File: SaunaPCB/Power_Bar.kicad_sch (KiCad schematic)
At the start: 54 parts, among them J201 KL3RM7.62, J202 KL3RM7.62, J203 KL3RM7.62, J204 KL2RM5.08, J205 KL3RM7.62, J206 KL3RM7.62, K201 Relais_SPDT_CO, K202 Relais_SPDT_CO, K203 Relais_SPDT_CO, K204 Relais_SPDT_CO, K205 Relais_SPDT_CO, K206 Relais_SPDT_CO, K207 Relais_SPDT_CO, U201 LHE05-20B24, U202 4N25, U203 4N25, U204 4N25, U302 LM2576T-5

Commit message: some step files added
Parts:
- renumbered C201 to C301, C202 to C302, C203 to C303, C204 to C304, C205 to C305, D201 to D301, D202 to D302, D301 to D303, D203 to D304, D204 to D305, D205 to D306, D206 to D307, D207 to D308, F201 to F301, H201 to H301, H202 to H302, H203 to H303, H204 to H304, H205 to H305, J201 to J301, J202 to J302, J203 to J303, J204 to J304, J205 to J305, J206 to J306, K201 to K301, K202 to K302, K203 to K303, K204 to K304, K205 to K305, K206 to K306, K207 to K307, L201 to L301, L202 to L302, L203 to L303, L203 to L304, R201 to R301, R202 to R302, R203 to R303, R204 to R304, R205 to R305, R206 to R306, R207 to R307, R208 to R308, R209 to R309, R210 to R310, R211 to R311, R212 to R312, R213 to R313, U201 to U301, U202 to U303, U203 to U304, U204 to U305
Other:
- moved on the sheet: D301, K301, K303, K305

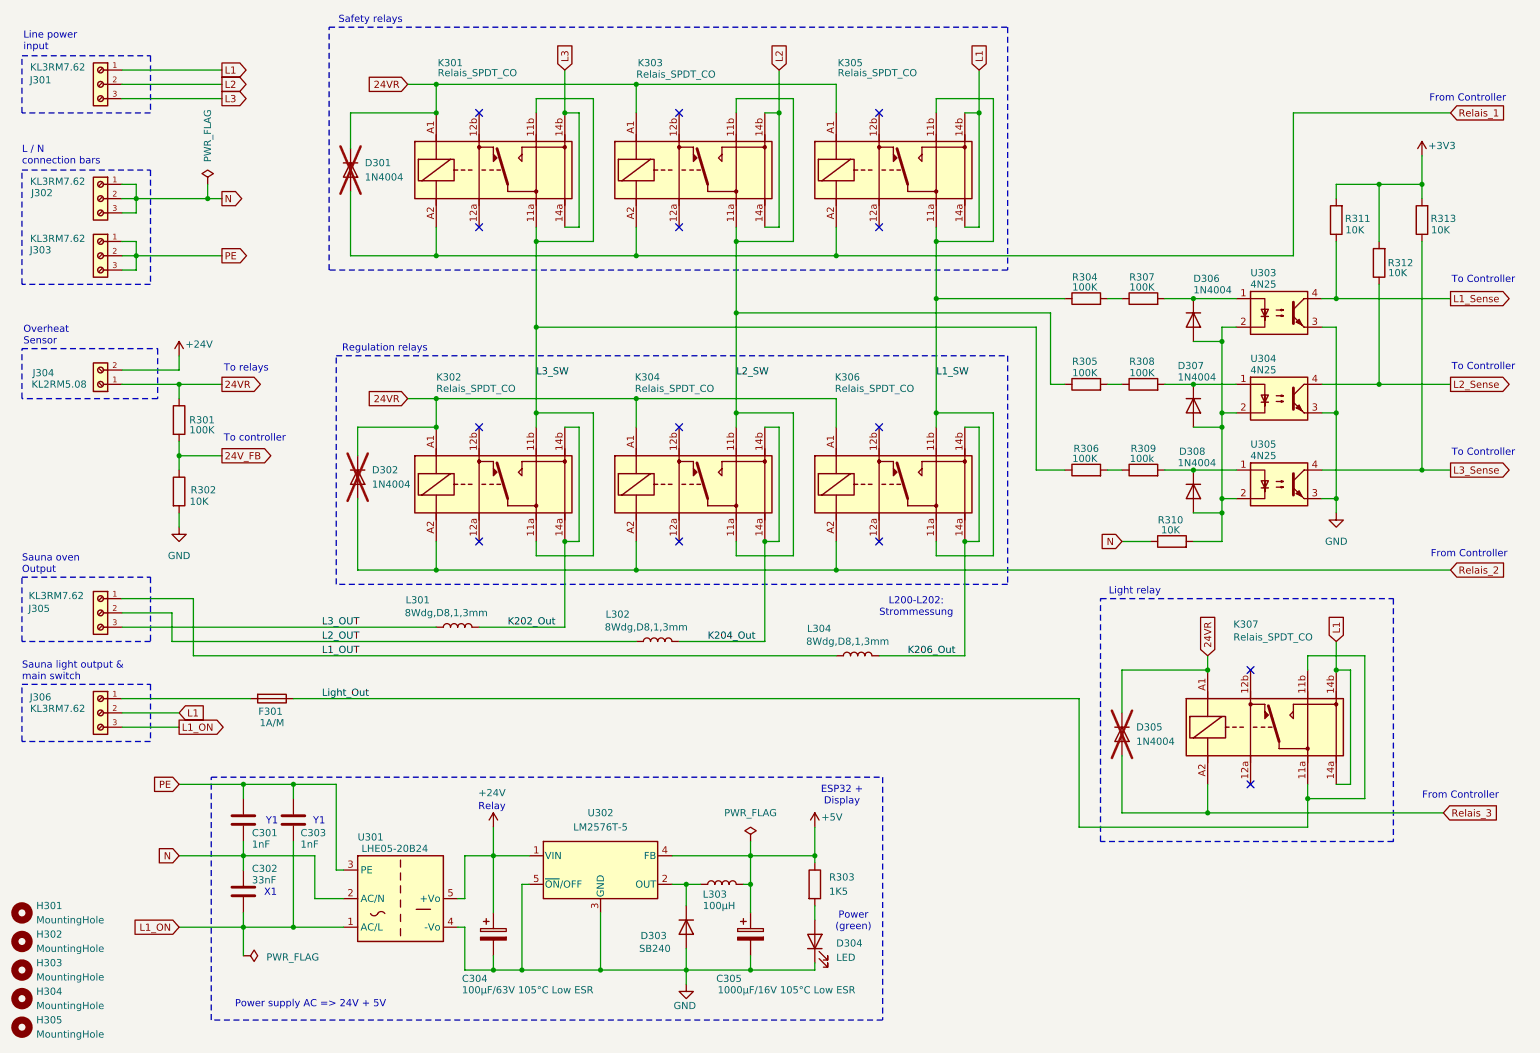
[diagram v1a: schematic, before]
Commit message: Hall sensors for current measurement added
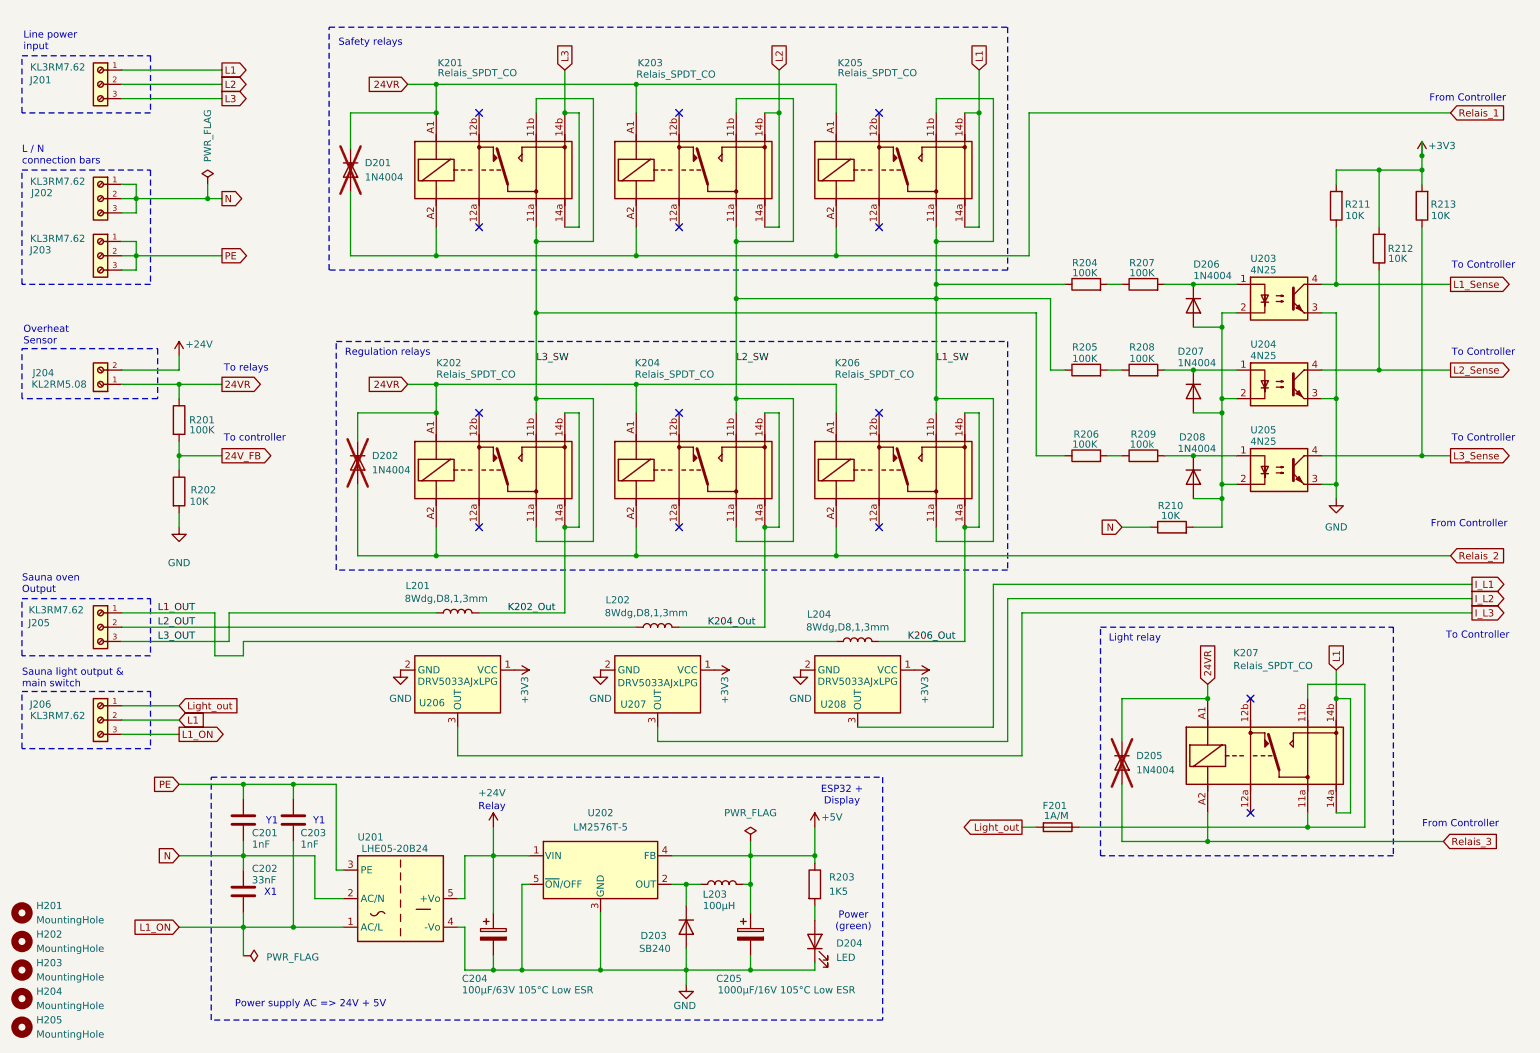
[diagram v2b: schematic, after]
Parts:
- added U206, U207, U208: DRV5033AJxLPG, Package_TO_SOT_THT:TO-92_Inline, symbol Sensor_Magnetic:DRV5033AJxLPG
- L201: renamed from L301; footprint SaunaProject:Current_Coil_15X14 -> SaunaProject:Current_Coil_19X14
- L202: renamed from L302; footprint SaunaProject:Current_Coil_15X14 -> SaunaProject:Current_Coil_19X14
- L204: renamed from L304; footprint SaunaProject:Current_Coil_15X14 -> SaunaProject:Current_Coil_19X14
- R210: renamed from R310; footprint Resistor_THT:R_Axial_DIN0207_L6.3mm_D2.5mm_P10.16mm_Horizontal -> Resistor_SMD:R_1206_3216Metric
- renumbered C301 to C201, C302 to C202, C303 to C203, C304 to C204, C305 to C205, D301 to D201, D302 to D202, D303 to D203, D304 to D204, D305 to D205, D306 to D206, D307 to D207, D308 to D208, F301 to F201, H301 to H201, H302 to H202, H303 to H203, H304 to H204, H305 to H205, J301 to J201, J302 to J202, J303 to J203, J304 to J204, J305 to J205, J306 to J206, K301 to K201, K302 to K202, K303 to K203, K304 to K204, K305 to K205, K306 to K206, K307 to K207, L303 to L203, R301 to R201, R302 to R202, R303 to R203, R304 to R204, R305 to R205, R306 to R206, R307 to R207, R308 to R208, R309 to R209, R311 to R211, R312 to R212, R313 to R213, U301 to U201, U302 to U202, U303 to U203, U304 to U204, U305 to U205
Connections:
- net L2_SW is gone; now on net L1_SW: K203.11a, K203.11b, K204.11a, K204.11b, R205.1
- net +3V3: now also U206.1 (VCC), U207.1 (VCC), U208.1 (VCC)
- net GND: now also U206.2 (GND), U207.2 (GND), U208.2 (GND)
- net Light_out: now reaches F201.2, J206.1
- net Light_Out: no longer names the net of F201.1, K207.11a, K207.11b
- new net I_L1: U208.3 (OUT)
- new net I_L2: U207.3 (OUT)
- new net I_L3: U206.3 (OUT)
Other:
- note removed: "L200-L202: Strommessung"
- moved on the sheet: D202, D205, D206, D207, D208, F201, J205, J206, K202, K204, K206, K207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

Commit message: Hall effect sensor type changed to DRV5053 .gitignore added: ignore .zip files in KiCAD backup folder
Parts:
- U206, U207, U208: value DRV5033AJxLPG -> DRV5053
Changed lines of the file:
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@@
 			)
 		)
-		(property "Value" "DRV5033AJxLPG"
+		(property "Value" "DRV5053"
 			(at 128.27 131.826 90)
 			(effects
@@
 			)
 		)
-		(property "Value" "DRV5033AJxLPG"
+		(property "Value" "DRV5053"
 			(at 163.83 131.572 90)
 			(effects
@@
 			)
 		)
-		(property "Value" "DRV5033AJxLPG"
+		(property "Value" "DRV5053"
 			(at 92.71 131.572 90)
 			(effects

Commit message: First routing almost finished Connector to LCD and encoder to be added!
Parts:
- added C206: 100nF, Capacitor_SMD:C_0805_2012Metric, symbol Device:C
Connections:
- net +3V3: now also C206.1
- net GND: now also C206.2
- net L1_SW: no longer K203.11a, K203.11b, K204.11a, K204.11b, R205.1
- new net L2_SW: K203.11a, K203.11b, K204.11a, K204.11b, R205.1

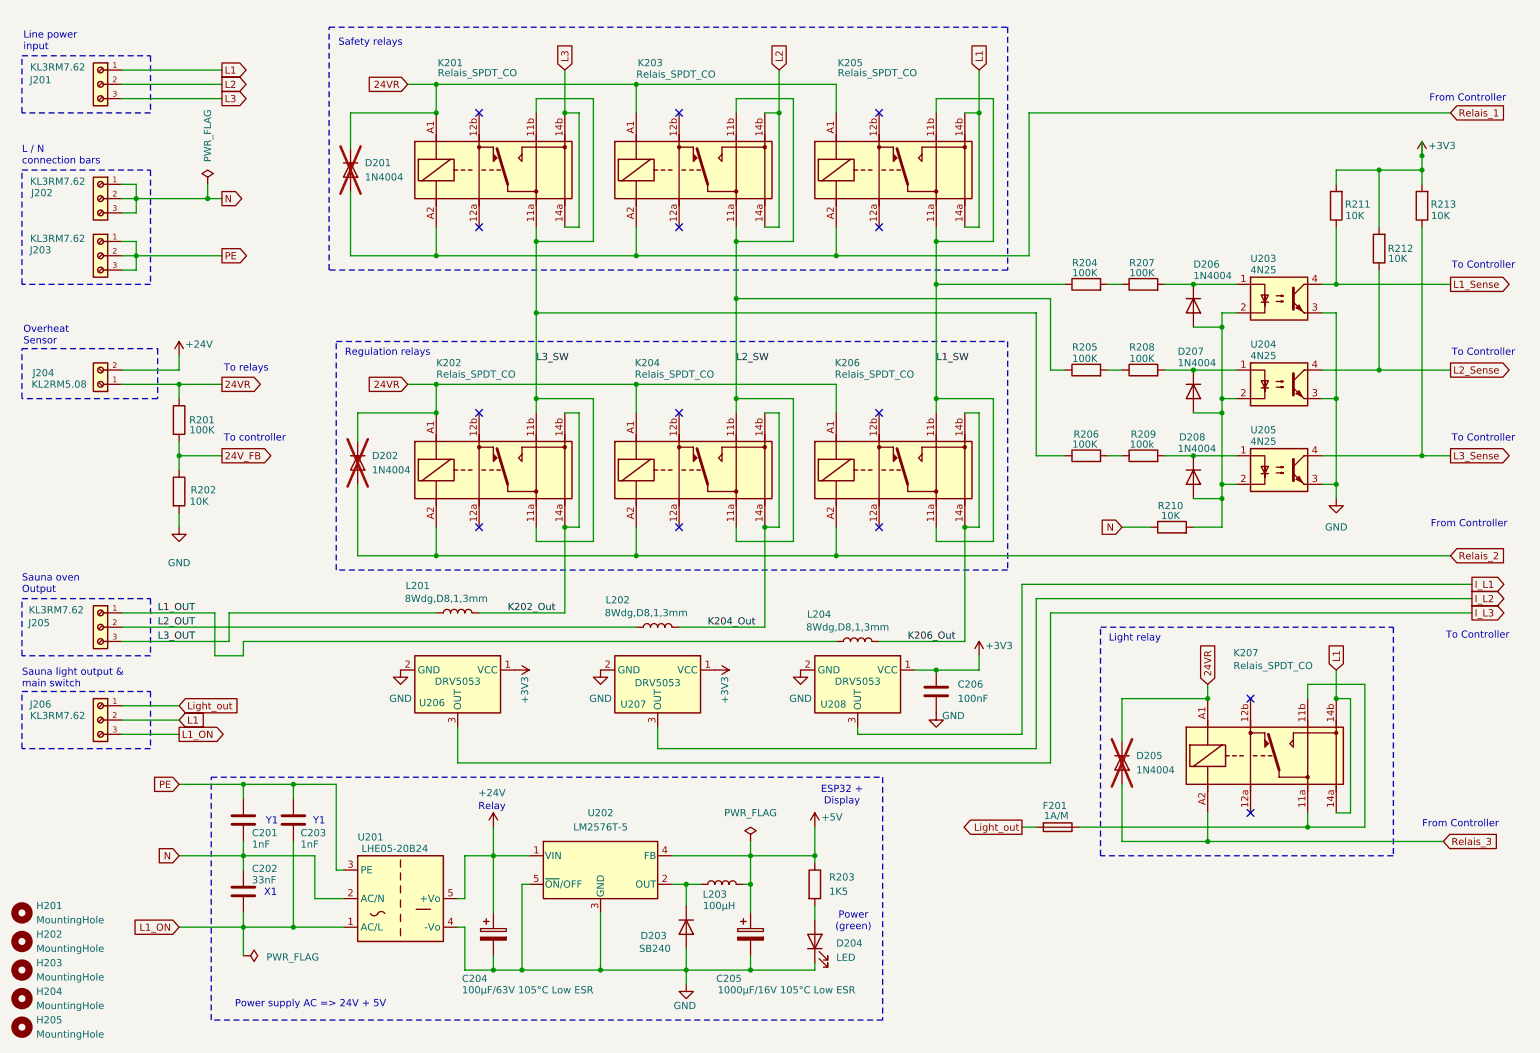
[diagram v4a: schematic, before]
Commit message: Usage ULN changed Top silkscreen PCB almost ready Values Diodes changed all 1N4004 => SG1 Relay diodes changed from NB to used (for security reasons; Diode in ULN may be not powerful enough)
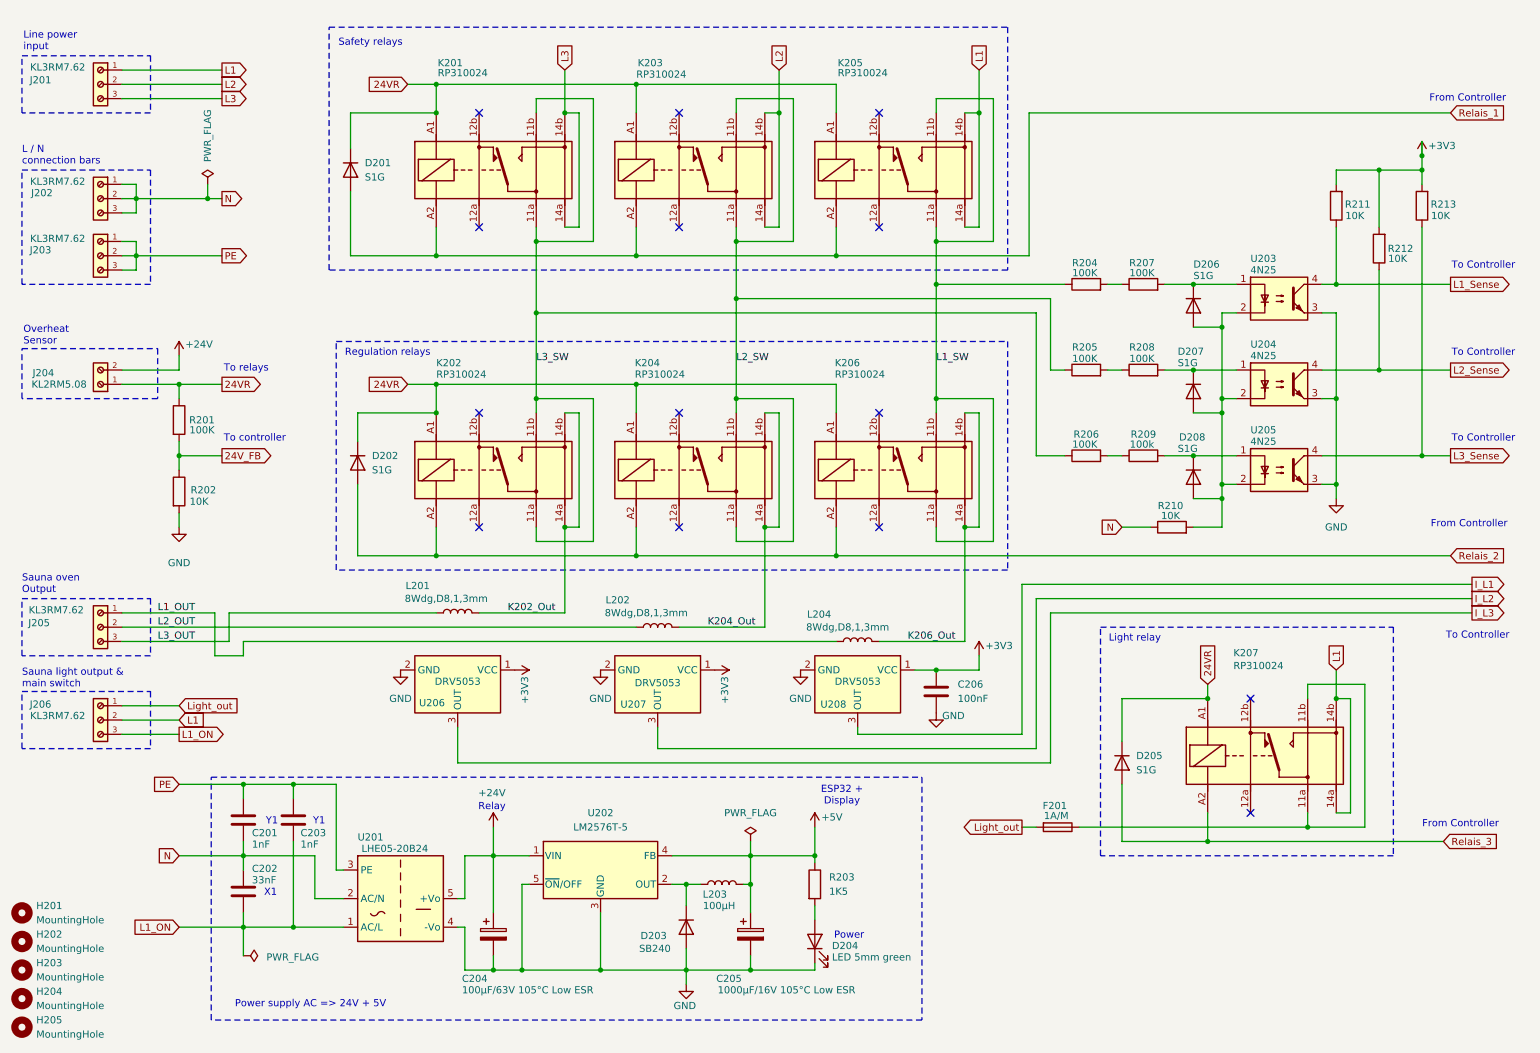
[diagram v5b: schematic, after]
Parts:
- D201, D202, D205: value 1N4004 -> S1G; now fitted
- D204: value LED -> LED 5mm green
- D206, D207, D208: value 1N4004 -> S1G
- K201, K202, K203, K204, K205, K206, K207: value Relais_SPDT_CO -> RP310024
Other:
- note added: "Power"
- note removed: "Power (green)"
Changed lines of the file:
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@@
 	(rectangle
 		(start 48.895 148.59)
-		(end 168.275 191.77)
+		(end 175.26 191.77)
 		(stroke
 			(width 0)
@@
 		)
 	)
-	(text "Power\n(green)"
+	(text "Power"
 		(exclude_from_sim no)
-		(at 163.068 174.244 0)
+		(at 162.306 176.784 0)
 		(effects
 			(font
@@
 		(in_bom yes)
 		(on_board yes)
-		(dnp yes)
+		(dnp no)
 		(fields_autoplaced yes)
 		(property "Reference" "D201"
@@
 			)
 		)
-		(property "Value" "1N4004"
+		(property "Value" "S1G"
 			(at 76.2 41.9099 90)
 			(effects
@@
 		(on_board yes)
 		(dnp no)
-		(fields_autoplaced yes)
 		(property "Reference" "D204"
-			(at 160.02 178.1174 90)
+			(at 159.258 178.562 90)
 			(effects
 				(font
@@
 			)
 		)
-		(property "Value" "LED"
-			(at 160.02 180.6574 90)
+		(property "Value" "LED 5mm green"
+			(at 159.258 180.594 90)
 			(effects
 				(font
@@
 			)
 		)
-		(property "Value" "1N4004"
+		(property "Value" "S1G"
 			(at 223.52 59.436 90)
 			(effects
@@
 			)
 		)
-		(property "Value" "Relais_SPDT_CO"
+		(property "Value" "RP310024"
 			(at 89.154 23.368 0)
 			(effects
@@
 			)
 		)
-		(property "Value" "Relais_SPDT_CO"
+		(property "Value" "RP310024"
 			(at 230.632 128.778 0)
 			(effects
@@
 		(in_bom yes)
 		(on_board yes)
-		(dnp yes)
+		(dnp no)
 		(fields_autoplaced yes)
 		(property "Reference" "D202"
@@
 			)
 		)
-		(property "Value" "1N4004"
+		(property "Value" "S1G"
 			(at 77.47 93.9799 90)
 			(effects
@@
 			)
 		)
-		(property "Value" "1N4004"
+		(property "Value" "S1G"
 			(at 220.726 74.93 90)
 			(effects
@@
 			)
 		)
-		(property "Value" "Relais_SPDT_CO"
+		(property "Value" "RP310024"
 			(at 159.766 76.962 0)
 			(effects
@@
 			)
 		)
-		(property "Value" "Relais_SPDT_CO"
+		(property "Value" "RP310024"
 			(at 124.46 23.622 0)
 			(effects
@@
 			)
 		)
-		(property "Value" "1N4004"
+		(property "Value" "S1G"
 			(at 220.726 90.17 90)
 			(effects
@@
 			)
 		)
-		(property "Value" "Relais_SPDT_CO"
+		(property "Value" "RP310024"
 			(at 124.206 76.962 0)
 			(effects
@@
 		(in_bom yes)
 		(on_board yes)
-		(dnp yes)
+		(dnp no)
 		(property "Reference" "D205"
 			(at 213.36 144.7799 90)
@@
 			)
 		)
-		(property "Value" "1N4004"
+		(property "Value" "S1G"
 			(at 213.36 147.3199 90)
 			(effects
@@
 			)
 		)
-		(property "Value" "Relais_SPDT_CO"
+		(property "Value" "RP310024"
 			(at 88.9 76.962 0)
 			(effects
@@
 			)
 		)
-		(property "Datasheet" ""
+		(property "Datasheet" "RP310024"
 			(at 99.06 93.98 0)
 			(effects
@@
 			)
 		)
-		(property "Value" "Relais_SPDT_CO"
+		(property "Value" "RP310024"
 			(at 160.274 23.368 0)
 			(effects
